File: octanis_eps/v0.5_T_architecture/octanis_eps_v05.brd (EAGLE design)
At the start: 80 x 50 mm, 141 parts, among them IC1 OPA2333DGK, Q3 32.768kHz, Q4 BSS123, U1 BQ24650_RVA_16, U10 CSD16327Q3_DQG_8, U13 CSD16327Q3_DQG_8, U14 CSD16327Q3_DQG_8, U2 Value, U3 Value, U4 Value, U5 TPS2022D, U6 TPS61232, U7 CSD16327Q3_DQG_8, U8 MSP430G2544, U9 CSD16327Q3_DQG_8

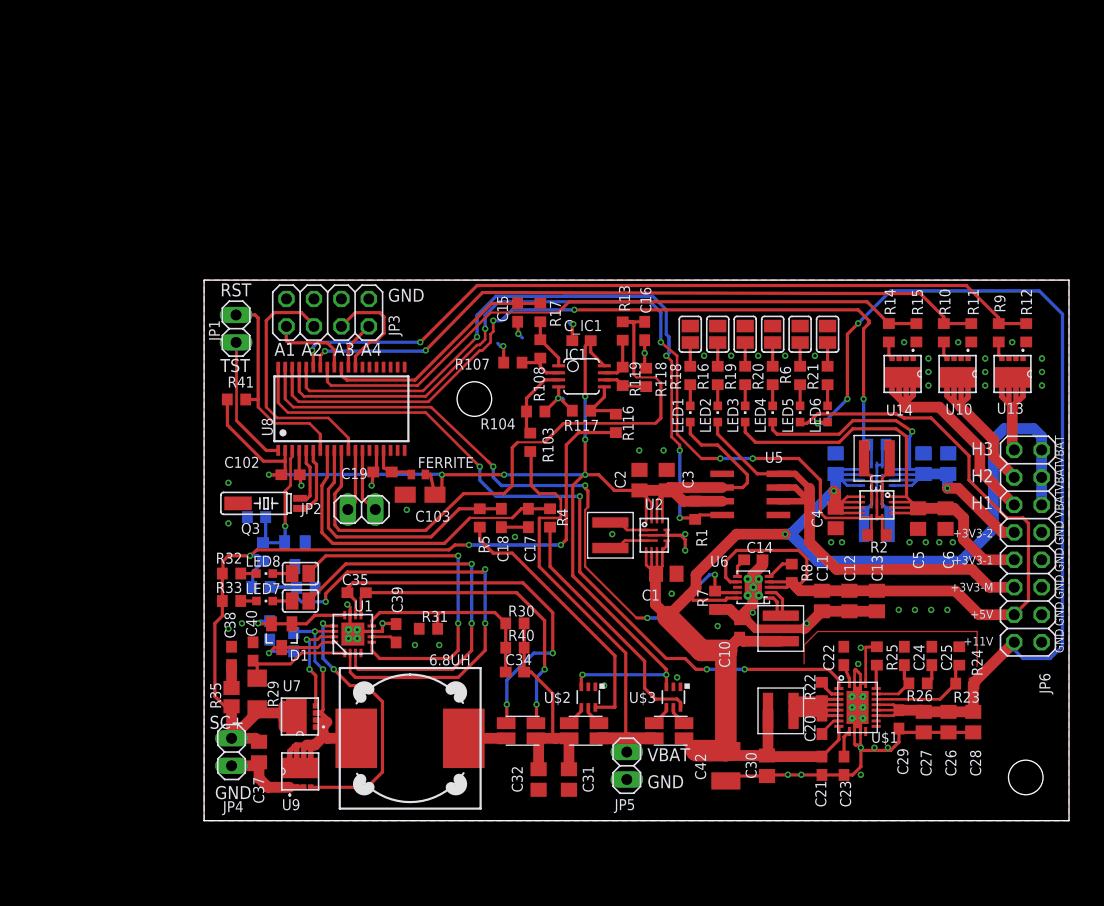
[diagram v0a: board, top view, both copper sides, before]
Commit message: Labels of EPS05 changed
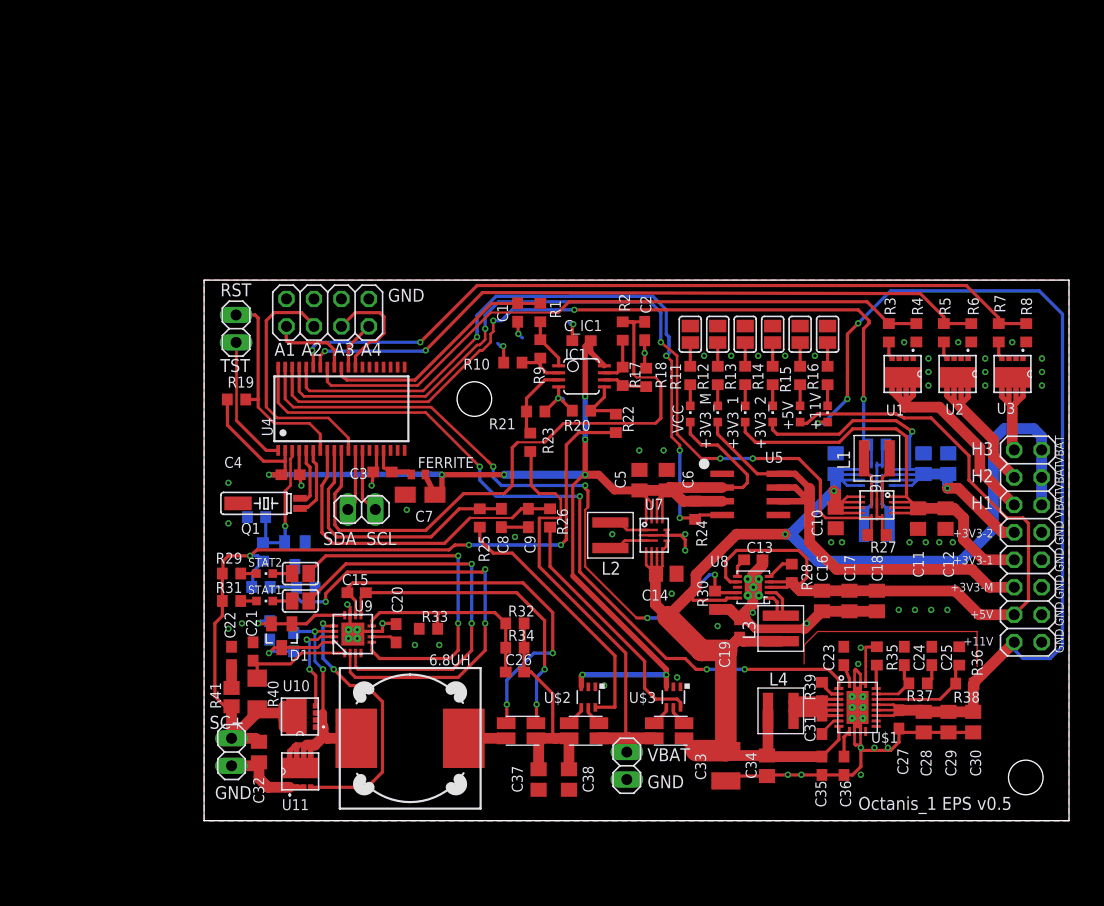
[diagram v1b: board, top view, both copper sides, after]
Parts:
- removed C39: 1uF, rcl:C0603
- removed C40: 1u, rcl:C0603
- removed C42: 47uF Tantal, rcl:C1210
- removed L5: 1.5uH, Coilcraft:XFL4020
- removed R107, R116, R118: 200k, rcl:R0603
- removed R108, R117, R119: 100k, rcl:R0603
- removed U13, U14: CSD16327Q3_DQG_8, texasinstruments:DQG8
- added C100: 100nF, rcl:C0603
- added C101: 1uF, rcl:C0603
- added C104: 10uF, resistor:C0805
- added L100: 1uH, Coilcraft:XFL4020
- added R100, R101: (no value), rcl:R0603
- added R102: 1M, rcl:R0603
- added R36: 56k, resistor:R0603
- added R37: 150-220k, resistor:R0603
- added R38: 470k, resistor:R0603
- added U100: Value, octanis_eps_v05:RNC0014A
- added U11: CSD16327Q3_DQG_8, texasinstruments:DQG8
- C1: value 10uF -> 1.5uF; device resistor:C0805 -> rcl:C0603
- C10: value 22uF -> 10uF; device rcl:C0603 -> resistor:C0805
- C102: value 100nF -> 22uF; device rcl:C0603 -> resistor:C0805
- C103: value 10uF -> 22uF; device rcl:A/3216-18R -> resistor:C0805
- C13: value 22uF -> 10nF; device resistor:C0805 -> rcl:C0603
- C14: value 10nF -> 10uF; device rcl:C0603 -> resistor:C0805
- C15: value 1.5uF -> 100nF
- C16, C17, C18: value 1.5uF -> 22uF; device rcl:C0603 -> resistor:C0805
- C19: value 100nF -> 22uF
- C2, C8, C9: value 22uF -> 1.5uF; device resistor:C0805 -> rcl:C0603
- C20: value 100nF -> 1uF
- C21: value 100nF -> 1u
- C23: value 47nF -> 2.2uF
- C26: value 22uF -> 22pF; device resistor:C0805 -> rcl:C0603
- C27: value 22uF -> 1uF; device resistor:C0805 -> rcl:C0603
- C29: value 1uF -> 22uF; device rcl:C0603 -> resistor:C0805
- C3: value 22uF -> 100nF; device resistor:C0805 -> rcl:C0603
- C30: value 10uF -> 22uF
- C31, C4: value 10uF -> 100nF; device resistor:C0805 -> rcl:C0603
- C33: value 1uF -> 47uF Tantal; device rcl:C0603 -> rcl:C1210
- C34: value 22pF -> 10uF; device rcl:C0603 -> resistor:C0805
- C36: value 100nF -> 47nF
- C38: value 2.2uF -> 10uF; device rcl:C0603 -> resistor:C0805
- C7: device resistor:C0805 -> rcl:A/3216-18R
- JP1: device Headerlibrary:1X02 -> Headerlibrary:2X04
- JP3: device Headerlibrary:2X04 -> Headerlibrary:1X02
- JP4: device Headerlibrary:1X02 -> Headerlibrary:2X08
- JP6: device Headerlibrary:2X08 -> Headerlibrary:1X02
- L4: value 1uH -> 1.5uH
- R1, R2, R3: value 1M -> 1k; device resistor:R0603 -> rcl:R0603
- R10, R18: value 1k -> 200k
- R103: value 200k -> 1M
- R104: value 100k -> 1M; device rcl:R0603 -> resistor:R0603
- R11, R12, R7: value 1M -> 1k
- R15: value 1M -> 1.5k
- R16: value 1k -> 4.7k
- R17, R20, R9: value 1k -> 100k
- R19: value 1k -> 10k
- R21: value 4.7k -> 100k
- R22: value 47k -> 200k; device resistor:R0603 -> rcl:R0603
- R23: value 470k -> 200k; device resistor:R0603 -> rcl:R0603
- R24: value 56k -> 1M
- R25: value 270k -> 1k; device resistor:R0603 -> rcl:R0603
- R26: value 150-220k -> 1k; device resistor:R0603 -> rcl:R0603
- R27: value (none) -> 1M; device rcl:R0603 -> resistor:R0603
- R28: value (none) -> 1M
- R29: value 10 -> 4k7; device rcl:R1206 -> rcl:R0603
- R30: value 100k -> 1M
- R31: value 100k -> 4k7
- R32, R33: value 4k7 -> 100k
- R34: value 1M -> 2.2M
- R35: value 2 -> 270k; device rcl:R2012 -> resistor:R0603
- R39: value 1M -> 47k; device rcl:R0603 -> resistor:R0603
- R4: value 1k -> 1M
- R40: value 2.2M -> 10; device rcl:R0603 -> rcl:R1206
- R41: value 10k -> 2; device rcl:R0603 -> rcl:R2012
- R6: value 1.5k -> 1M
- R_SENSE1: value RSENSE1 -> RSENSE1 10mOhm
- R_SENSE2: value RSENSE1 10mOhm -> RSENSE1
- U1: value BQ24650_RVA_16 -> CSD16327Q3_DQG_8; device octanis_eps_v05:RVA16_2P14X2P14 -> texasinstruments:DQG8
- U2, U3: value Value -> CSD16327Q3_DQG_8; device octanis_eps_v05:RNC0014A -> texasinstruments:DQG8
- U4: value Value -> MSP430G2544; device octanis_eps_v05:RNC0014A -> Octanis1_EPS:TSSOP38_MSPGXX44_SERIES
- U6: value TPS61232 -> Value; device texasinstruments:S-PVSON-N10 -> octanis_eps_v05:RNC0014A
- U7: value CSD16327Q3_DQG_8 -> Value; device texasinstruments:DQG8 -> octanis_eps_v05:RNC0014A
- U8: value MSP430G2544 -> TPS61232; device Octanis1_EPS:TSSOP38_MSPGXX44_SERIES -> texasinstruments:S-PVSON-N10
- U9: value CSD16327Q3_DQG_8 -> BQ24650_RVA_16; device texasinstruments:DQG8 -> octanis_eps_v05:RVA16_2P14X2P14
- moved JP4 76.1 mm to (76.2, 25.4)
- moved U10 68.6 mm to (8.86, 9.64), turned to 180 degrees
- moved C102 60.8 mm to (68.8, 33.0), flipped to the bottom, turned to 90 degrees
- moved R35 59.8 mm to (62.2, 15.2)
- moved R27 57.2 mm to (62.2, 26.4), flipped to the top
- moved C22 56.6 mm to (2.54, 15.2)
- moved U1 56.3 mm to (64.6, 41.3), turned to 270 degrees
- moved C21 53.7 mm to (4.53, 15.7), turned to 90 degrees
- moved R39 53.3 mm to (57.1, 11.9), flipped to the top
- moved C36 52.2 mm to (59.2, 5.08), flipped to the top
- moved C4 50.6 mm to (8.00, 32.0), turned to 0 degrees
- moved U4 49.9 mm to (12.7, 38.1), flipped to the top, turned to 0 degrees
- moved R19 47.1 mm to (3.00, 39.0), turned to 180 degrees
- moved C103 46.6 mm to (66.5, 33.0), flipped to the bottom, turned to 90 degrees
- moved R5 46.2 mm to (68.4, 45.1), turned to 90 degrees
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- renumbered LED1 to VCC, LED2 to +3V3_M, LED3 to +3V3_1, LED4 to +3V3_2, LED5 to +5V, LED6 to +11V, LED7 to STAT1, LED8 to STAT2, Q3 to Q1, Q4 to Q100
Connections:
- net +12V: now also C30.2, JP4.2, R38.2; no longer C26.2, JP6.2, R23.2
- net +3V3: now also C4.1, C5.1, C6.1, C7.+, R19.2, R24.2, U4.2, U7.11, U7.12, U7.13, U7.14; no longer C102.1, C103.+, C2.1, C3.1, R1.2, R41.2, U2.11, U2.12, U2.13, U2.14, U8.2
- net +3V3_1: now also C11.1, C12.1, JP4.8, U6.11, U6.12, U6.13, U6.14; no longer C5.1, C6.1, JP6.8, U3.11, U3.12, U3.13, U3.14
- net +3V3_2: now also C102.1, C103.1, JP4.10, U100.11, U100.12, U100.13, U100.14; no longer C8.1, C9.1, JP6.10, U4.11, U4.12, U4.13, U4.14
- net +3V3_M: now also JP4.6; no longer JP6.6
- net +5V: now also C16.1, C17.1, C18.1, JP4.4, R28.2, U8.3, U8.4, U8.7; no longer C11.1, C12.1, C13.1, JP6.4, R8.2, U6.3, U6.4, U6.7
- net A_EXT1: now also JP1.1, U4.30; no longer JP3.1, U8.30
- net A_EXT2: now also JP1.3, U4.11; no longer JP3.3, U8.11
- net A_EXT3: now also JP1.5, U4.27; no longer JP3.5, U8.27
- net A_EXT4: now also JP1.7, U4.28; no longer JP3.7, U8.28
- net BAT+: now also JP6.2, R23.2, R_SENSE2.I1; no longer JP5.2, R103.2, R_SENSE1.I1
- net BAT_OUT: now also C104.1, C14.1, C19.1, C33.1, C34.1, C35.1, JP4.11, JP4.13, JP4.15, L3.P$1, L4.P$1, R_SENSE2.I2, U100.4, U100.5, U100.6, U100.7, U6.4, U6.5, U6.6, U6.7, U7.4, U7.5, U7.6, U7.7, U7.8, U8.10; no longer C1.1, C21.1, C30.1, C4.1, C42.1, C7.1, JP6.11, JP6.13, JP6.15, L1.P$1, L5.P$1, R_SENSE1.I2, U2.4, U2.5, U2.6, U2.7, U2.8, U3.4, U3.5, U3.6, U3.7, U4.4, U4.5, U4.6, U4.7, U6.10
- net EN_12V: now also U4.38; no longer U8.38
- net EN_3V3_1: now also R27.1, U4.35, U6.8; no longer R2.1, U3.8, U8.35
- net EN_3V3_2: now also R104.1, U100.8, U4.36; no longer R3.1, U4.8, U8.36
- net EN_3V3_M: now also R24.1, U4.34; no longer R1.1, U8.34
- net EN_5V: now also R30.2, U4.37, U8.9; no longer R7.2, U6.9, U8.37
- net EN_HEAT1: now also R3.2, R4.1, U4.31; no longer R14.2, R15.1, U8.31
- net EN_HEAT2: now also R5.2, R6.1, U4.32; no longer R10.2, R11.1, U8.32
- net EN_HEAT3: now also R7.2, R8.1, U4.33; no longer R12.1, R9.2, U8.33
- net EN_SC: now also R102.1, R103.2, U4.3; no longer R34.2, R39.1, U8.3
- net GND: now also C1.1, C101.2, C103.2, C104.2, C16.2, C17.2, C18.2, C2.1, C20.2, C30.1, C32.1, C34.2, C35.2, C36.2, C37.2, C7.-, C8.1, C9.1, JP1.2, JP1.4, JP1.6, JP1.8, JP4.3, JP4.5, JP4.7, JP4.9, R10.2, R100.1, R103.1, R104.2, R18.2, R20.1, R21.1, R27.2, R30.1, R33.1, R35.1, R36.1, R4.2, R6.2, R8.2, U1.1, U1.2, U1.3, U100.10, U100.2, U100.9, U11.1, U11.2, U11.3, U2.1, U2.3, U3.1, U3.3, U4.15, U4.4, U6.10, U6.2, U6.9, U7.10, U7.2, U7.9, U8.EXPAD, U8.GND1, U8.GND2, U8.GND3, U8.GND4, U8.GND5, U9.11, U9.17, U9.7, U9.V, U9.V_1, U9.V_2, U9.V_3; no longer C1.2, C103.-, C15.1, C16.1, C17.1, C18.1, C2.2, C26.1, C30.2, C31.2, C32.2, C37.1, C39.2, C40.2, C42.2, C7.2, C8.2, C9.2, JP3.2, JP3.4, JP3.6, JP3.8, JP6.3, JP6.5, JP6.7, JP6.9, R104.1, R107.2, R11.2, R117.1, R118.2, R12.2, R15.2, R2.2, R24.1, R25.1, R28.1, R3.2, R31.1, R34.1, R7.1, U1.11, U1.17, U1.7, U1.V, U1.V_1, U1.V_2, U1.V_3, U10.1, U10.2, U10.3, U13.1, U13.2, U13.3, U14.1, U14.2, U14.3, U2.10, U2.9, U3.10, U3.9, U4.10, U4.2, U4.9, U6.EXPAD, U6.GND1, U6.GND2, U6.GND3, U6.GND4, U6.GND5, U8.15, U8.4, U9.1, U9.2, U9.3
- net HEAT1: now also JP4.12, U1.5, U1.6, U1.7, U1.8; no longer JP6.12, U14.5, U14.6, U14.7, U14.8
- net HEAT2: now also JP4.14, U2.5, U2.6, U2.7, U2.8; no longer JP6.14, U10.5, U10.6, U10.7, U10.8
- net HEAT3: now also JP4.16, U3.5, U3.6, U3.7, U3.8; no longer JP6.16, U13.5, U13.6, U13.7, U13.8
- net I2C_SCL: now also JP3.2, U4.13; no longer JP2.2, U8.13
- net I2C_SDA: now also JP3.1, U4.12; no longer JP2.1, U8.12
- net IND: now also L3.P$2, U8.1, U8.2; no longer L1.P$2, U6.1, U6.2
- net I_IN: now also C8.2, R25.1, U4.9; no longer C18.2, R5.1, U8.9
- net I_OUT: now also C9.2, R26.1, U4.8; no longer C17.2, R4.1, U8.8
- net LED5: now also R15.2; no longer R6.2
- net N$1: now also U7.3; no longer U2.3
- net N$11: now also L100.P$1, U100.3; no longer L4.P$1, U4.3
- net N$12: now also L100.P$2, U100.1; no longer L4.P$2, U4.1
- net N$14: now also R15.1; no longer R6.1
- net N$19: now also R1.2, R9.1; no longer R108.1, R17.2
- net N$2: now also R28.1, U8.5; no longer R8.1, U6.5
- net N$20: now also R10.1, R9.2; no longer R107.1, R108.2
- net N$21: now also R21.2, R23.1; no longer R103.1, R104.2
- net N$22: now also R17.1, R2.2; no longer R119.1, R13.2
- net N$23: now also R17.2, R18.1; no longer R118.1, R119.2
- net N$24: now also R20.2, R22.1; no longer R116.1, R117.2
- net N$25: now also R26.2; no longer R4.2
- net N$26: now also R25.2; no longer R5.2
- net N$27: now also R7.1, U3.4; no longer R9.1, U13.4
- net N$3: now also U7.1; no longer U2.1
- net N$30: now also U4.6; no longer U8.6
- net N$31: now also R5.1, U2.4; no longer R10.1, U10.4
- net N$32: now also R_SENSE2.V1; no longer R_SENSE1.V1
- net N$33: now also R_SENSE2.V2; no longer R_SENSE1.V2
- net N$36: now also U4.5; no longer U8.5
- net N$37: now also R3.1, U1.4; no longer R14.1, U14.4
- net N$38: now also C31.2; no longer C20.2
- net N$39: now also R12.2; no longer R16.2
- net N$4: now also R_SENSE1.I1; no longer R_SENSE2.I1
- net N$40: now also R12.1; no longer R16.1
- net N$43: now also R11.2; no longer R18.2
- net N$45: now also R11.1; no longer R18.1
- net N$46: now also R14.2; no longer R20.2
- net N$47: now also R14.1; no longer R20.1
- net N$48: now also R16.2; no longer R21.2
- net N$49: now also R16.1; no longer R21.1
- net N$5: now also C13.1, U8.6; no longer C14.1, U6.6
- net N$50: now also C31.1, L4.P$2, R39.2; no longer C20.1, L5.P$2, R22.2
- net N$51: now also R13.2; no longer R19.2
- net N$52: now also R13.1; no longer R19.1
- net N$53: now also R39.1; no longer R22.1
- net N$54: now also R37.1; no longer R26.1
- net N$56: now also C36.1; no longer C23.1
- net N$57: now also R35.2; no longer R25.2
- net N$58: now also R37.2; no longer R26.2
- net N$59: now also C23.1; no longer C22.1
- net N$6: now also L1.P$1, U6.3; no longer L3.P$1, U3.3
- net N$60: now also R36.2, R38.1; no longer R23.1, R24.2
- net N$64: now also R100.2, R101.1, U9.2; no longer R27.1, R28.2, U1.2
- net N$65: now also C22.1, R41.1; no longer C38.1, R35.1
- net N$66: now also R31.1; no longer R33.1
- net N$67: now also J7.2; no longer J8.2
- net N$68: now also J8.2; no longer J7.2
- net N$69: now also R29.1; no longer R32.1
- net N$7: now also L1.P$2, U6.1; no longer L3.P$2, U3.1
- net N$70: now also J7.1, U9.5; no longer J8.1, U1.5
- net N$71: now also J8.1, U9.3; no longer J7.1, U1.3
- net N$72: now also C20.1, U9.6; no longer C39.1, U1.6
- net N$73: now also C21.1, R40.2, U9.1; no longer C40.1, R29.2, U1.1
- net N$75: now also JP2.2, U4.1; no longer JP1.2, U8.1
- net N$76: now also C100.1, U10.1, U10.2, U10.3, U11.5, U11.6, U11.7, U11.8, U9.14; no longer C36.1, U1.14, U7.1, U7.2, U7.3, U9.5, U9.6, U9.7, U9.8
- net N$77: now also C15.2, R_SENSE1.V1, U9.10; no longer C35.2, R_SENSE2.V1, U1.10
- net N$78: now also C15.1, R_SENSE1.V2, U9.9; no longer C35.1, R_SENSE2.V2, U1.9
- net N$80: now also U10.4, U9.15; no longer U1.15, U7.4
- net N$81: now also U11.4, U9.13; no longer U1.13, U9.4
- net N$82: now also C26.2, R32.1, R33.2, R34.1, U9.8; no longer C34.2, R30.1, R31.2, R40.1, U1.8
- net N$84: now also C101.1, U9.12; no longer C33.1, U1.12
- net N$85: now also C100.2, U9.16; no longer C36.2, U1.16
- net N$93: now also JP2.1, R19.1, U4.7; no longer JP1.1, R41.1, U8.7
- net N$99: now also C3.1, U4.16; no longer C19.1, U8.16
- net SC+: now also C32.2, JP5.2, R101.2, R102.2, R22.2, R29.2, R31.2, R40.1, R41.2, U10.5, U10.6, U10.7, U10.8; no longer C37.2, JP4.2, R116.2, R27.2, R29.1, R32.2, R33.2, R35.2, R39.2, U7.5, U7.6, U7.7, U7.8
- net SC_OUT: now also C26.1, C37.1, C38.1, R32.2, R34.2, R_SENSE1.I2; no longer C31.1, C32.1, C34.1, R30.2, R40.2, R_SENSE2.I2
- net V_BAT: now also C1.2, R1.1, U4.29; no longer C15.2, R17.1, U8.29
- net V_SC: now also C2.2, R2.1, U4.10; no longer C16.2, R13.1, U8.10
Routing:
- net N$76: track 28.0 -> 26.9 mm
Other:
- board text added: "L1"
- board text added: "L100"
- board text added: "L2"
- board text added: "L3"
- board text added: "L4"
- board text added: "Octanis_1 EPS v0.5"
- board text added: "SCL"
- board text added: "SDA"

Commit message: corrected eps libraries so that they are GERBER-izable. (ERROR was: 'Board contains a polygon that may cause extremely large plot data' and is due to drawn polygons with width=0 in tStop, tCream and top layers. They should never be used, instead draw rectangles or polygons with width>0
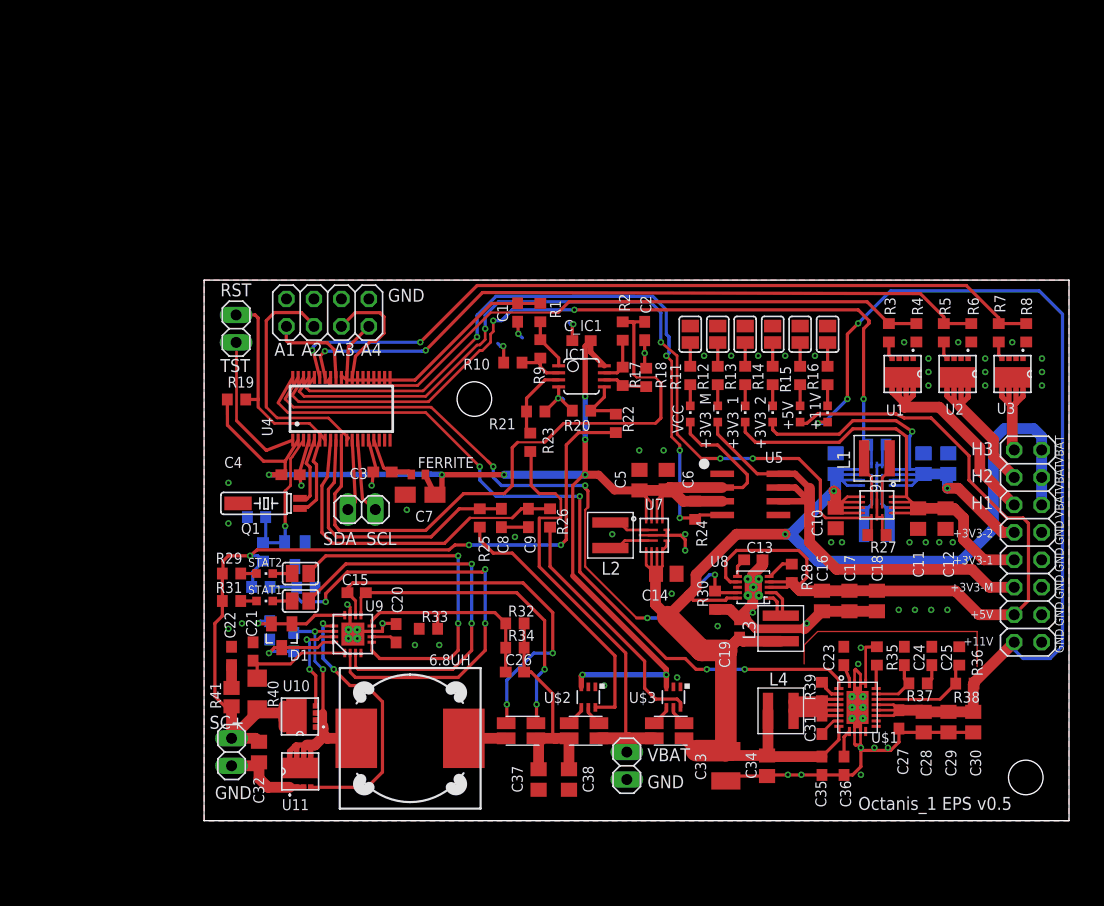
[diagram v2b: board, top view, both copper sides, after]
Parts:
- U4: device Octanis1_EPS:TSSOP38_MSPGXX44_SERIES -> Octanis1_EPS:TSSOP38
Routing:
- net GND: track 124.1 -> 126.3 mm
- net N$75: track 12.2 -> 13.8 mm
- net +3V3: track 139.0 -> 140.3 mm
- net EN_SC: track 13.3 -> 14.6 mm
- net N$99: track 4.37 -> 5.47 mm
- net N$36: track 5.43 -> 6.51 mm
- net N$30: track 6.52 -> 7.56 mm
- net EN_HEAT3: track 72.0 -> 73.0 mm
- net EN_HEAT2: track 65.2 -> 66.2 mm
- net A_EXT3: track 10.7 -> 11.6 mm
- net I2C_SCL: track 6.03 -> 6.99 mm
- net I_OUT: track 30.6 -> 31.5 mm
- net I2C_SDA: track 5.76 -> 6.72 mm
- net A_EXT1: track 7.73 -> 8.68 mm
- net A_EXT4: track 4.55 -> 5.51 mm
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
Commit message: replaced 3.3v converters to the BGA component. started moving components to make space on top side
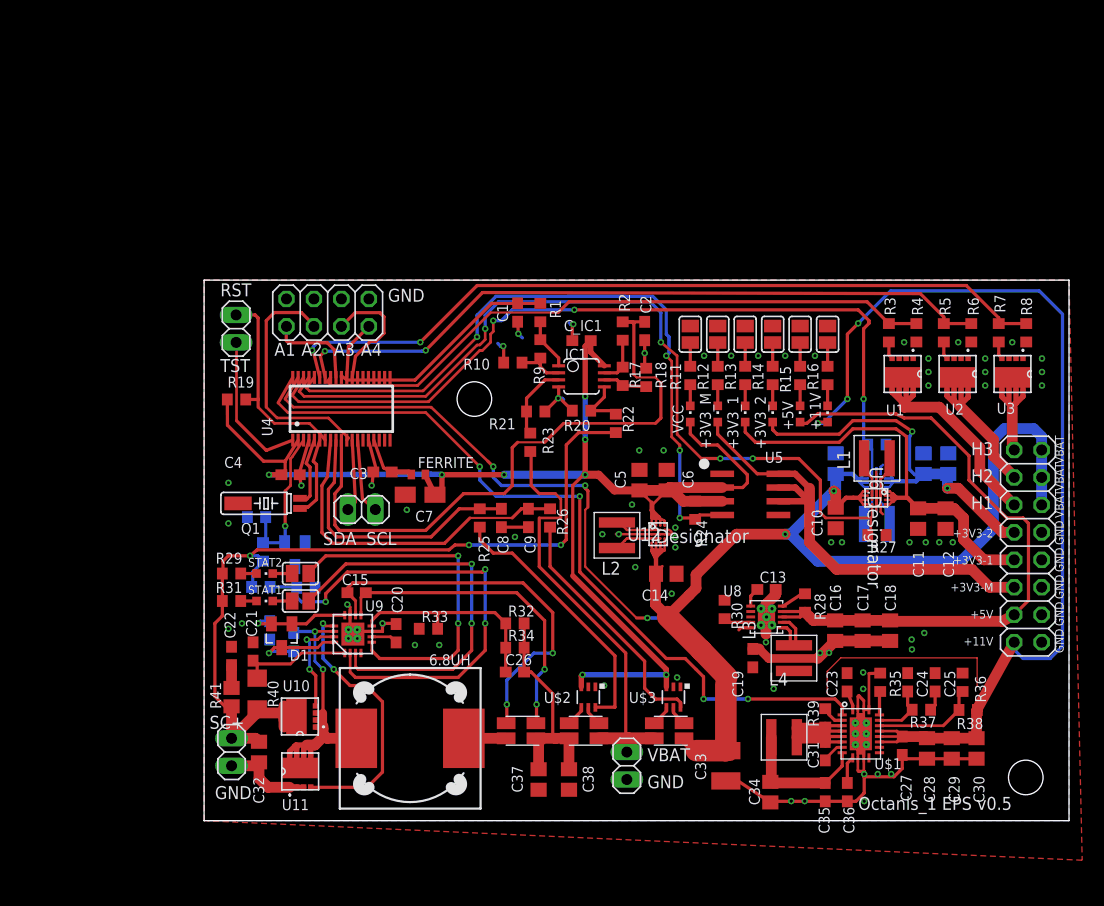
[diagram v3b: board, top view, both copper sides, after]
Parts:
- removed U100: Value, octanis_eps_v05:RNC0014A
- added U12: TPS630250YFFT, texasinstruments:YFF0020AEBA
- U6, U7: value Value -> TPS630250YFFT; device octanis_eps_v05:RNC0014A -> texasinstruments:YFF0020AEBA
- moved U7 21.2 mm to (62.2, 31.5), flipped to the bottom, turned to 90 degrees
- moved C16 3.00 mm to (58.4, 17.6)
- moved C17 3.00 mm to (60.9, 17.6)
- moved C18 3.00 mm to (63.4, 17.6)
- moved C19 3.00 mm to (50.7, 15.0)
- moved C13 3.00 mm to (52.0, 21.4)
- moved L3 3.00 mm to (54.6, 15.0)
- moved R28 3.00 mm to (55.6, 20.1)
- moved U8 3.00 mm to (52.0, 18.8)
- moved C34 2.46 mm to (52.4, 2.64)
- moved C35 2.46 mm to (57.5, 2.64)
- moved C36 2.46 mm to (59.5, 2.64)
- moved C23 2.46 mm to (59.5, 12.8)
- moved C24 2.46 mm to (65.1, 12.8)
- moved C25 2.46 mm to (67.6, 12.8)
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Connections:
- net +3V3: now also U12.1, U12.2, U12.3, U12.4; no longer U7.11, U7.12, U7.13, U7.14
- net +3V3_1: now also U6.1, U6.2, U6.3, U6.4; no longer U6.11, U6.12, U6.13, U6.14
- net +3V3_2: now also U7.1, U7.2, U7.3, U7.4; no longer U100.11, U100.12, U100.13, U100.14
- net BAT_OUT: now also U12.16, U12.17, U12.18, U12.19, U12.20, U6.17, U6.18, U6.19, U6.20, U7.17, U7.18, U7.19, U7.20; no longer U100.4, U100.5, U100.6, U100.7, U6.4, U6.5, U6.6, U6.7, U7.4, U7.5, U7.6, U7.7, U7.8
- net EN_3V3_1: now also U6.16; no longer U6.8
- net EN_3V3_2: now also U7.16; no longer U100.8
- net GND: now also U12.10, U12.11, U12.12, U12.8, U12.9, U6.11, U6.12, U6.8, U7.11, U7.12, U7.8; no longer U100.10, U100.2, U100.9, U6.2, U7.2
- net N$1: now also U12.13, U12.14, U12.15; no longer U7.3
- net N$11: now also U7.13, U7.14, U7.15; no longer U100.3
- net N$12: now also U7.5, U7.6, U7.7; no longer U100.1
- net N$3: now also U12.5, U12.6, U12.7; no longer U7.1
- net N$6: now also U6.13, U6.14, U6.15; no longer U6.3
- net N$7: now also U6.5, U6.6, U6.7; no longer U6.1
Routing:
- net BAT_OUT: track 150.2 -> 128.2 mm
- net +5V: track 76.2 -> 60.3 mm
- net EN_5V: track 60.9 -> 53.7 mm, vias 4 -> 3
- net +3V3_2: track 42.2 -> 38.8 mm
- net EN_12V: track 70.8 -> 73.3 mm
- net N$8: track 21.5 -> 19.1 mm
- net N$1: track 4.72 -> 6.52 mm
- net +12V: track 91.4 -> 93.2 mm
- net N$3: track 4.56 -> 6.27 mm
- net EN_3V3_1: track 77.3 -> 78.4 mm
- net EN_3V3_2: track 74.5 -> 75.3 mm
- net N$7: track 4.11 -> 4.67 mm
- net GND: track 126.3 -> 126.8 mm, vias 63 -> 67
- net N$12: track 4.11 -> 4.63 mm
- net N$6: track 4.08 -> 4.59 mm
